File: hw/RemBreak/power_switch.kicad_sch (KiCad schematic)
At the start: 33 parts, among them IC1 LTC2943IDD#TRPBF, IC2 MAX17049G+T10, Q10 BC337, Q11 BC847, Q12 Si7141DP, Q13 BC337, Q14 BC847, U2 INA219BxDCN, U6 BD4830FVE-TR

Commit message: reorganized subsheets
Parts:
- removed C1: 0.1uF, symbol Device:C_Polarized
- removed C5: 100nF, symbol Device:C
- removed IC1: LTC2943IDD#TRPBF, SON50P300X300X80-9N-D, symbol dodo-device:LTC2943IDD#TRPBF
- removed IC2: MAX17049G+T10, Package_DFN_QFN:TDFN-8-1EP_2x2mm_P0.5mm_EP0.8x1.2mm, symbol dodo-power:MAX17049G+T10
- removed R16, R18: 10, symbol Device:R
- removed R19, R23: 10k, symbol Device:R
- removed U2: INA219BxDCN, Package_TO_SOT_SMD:SOT-23-8, symbol Analog_ADC:INA219BxDCN
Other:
- note removed: "BATTERY SoC IC I2C address: 0x36 + R/W"
- note removed: "CURRENT SENSOR I2C address: 0x40 + R/W"

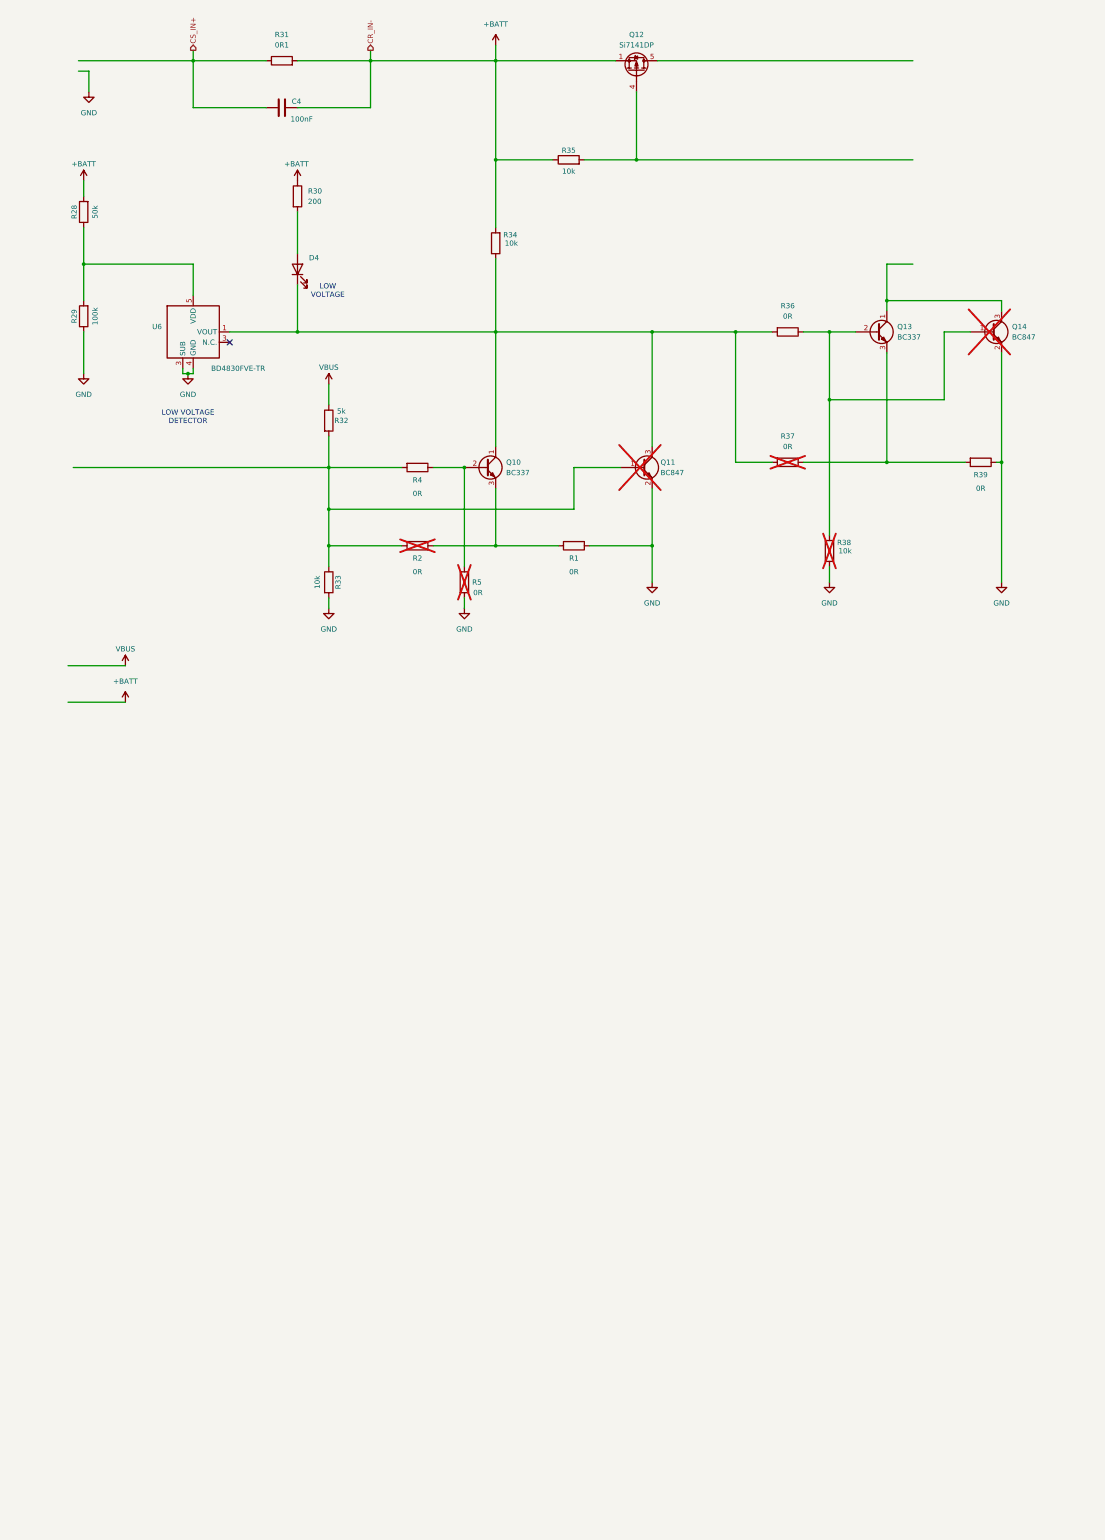
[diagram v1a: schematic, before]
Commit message: project update - started drawing the first revision of the board
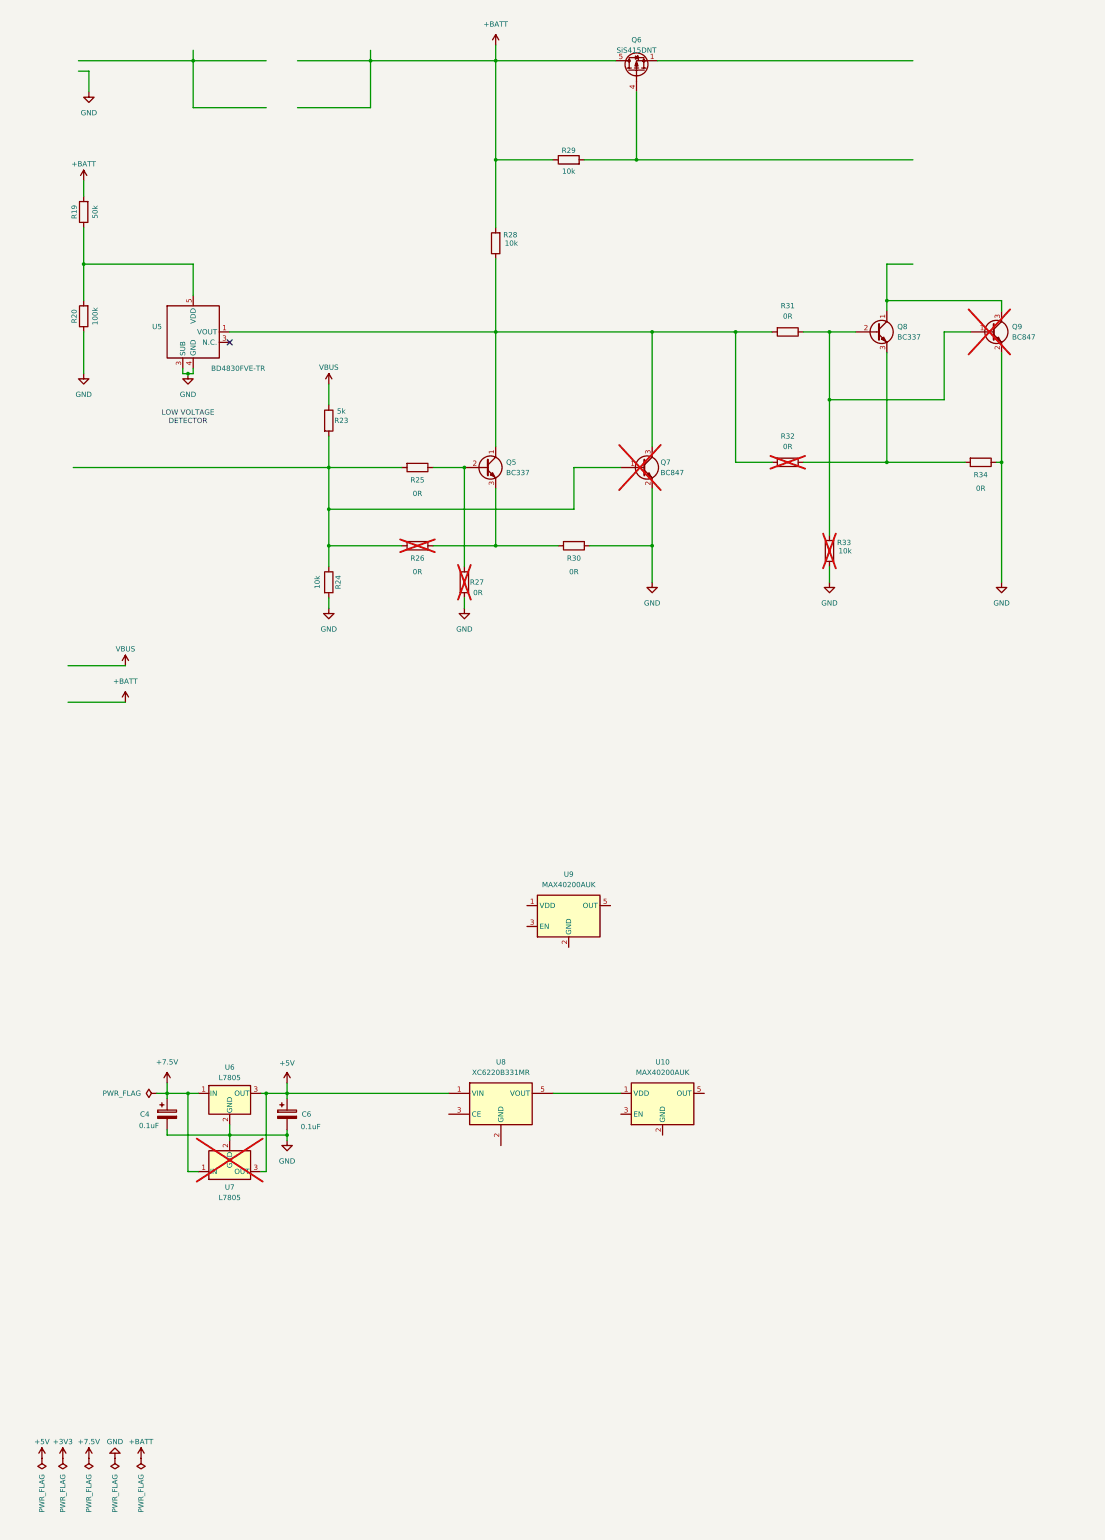
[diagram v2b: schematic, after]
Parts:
- removed C4: 100nF, symbol Device:C
- removed D4: LED, symbol Device:LED
- removed Q12: Si7141DP, Package_SO:PowerPAK_SO-8_Single, symbol Transistor_FET:Si7141DP
- removed R30: 200, symbol Device:R
- removed R31: 0R1, symbol Device:R
- added C4, C6: 0.1uF, Capacitor_SMD:C_0805_2012Metric, symbol Device:C_Polarized
- added Q6: SiS415DNT, Package_SO:Vishay_PowerPAK_1212-8_Single, symbol Transistor_FET:SiS415DNT
- added U10, U9: MAX40200AUK, Package_TO_SOT_SMD:SOT-23-5, symbol Analog_Switch:MAX40200AUK
- added U6: L7805, Package_TO_SOT_SMD:TO-263-2, symbol Regulator_Linear:L7805
- added U7: L7805, Package_TO_SOT_THT:TO-220-3_Horizontal_TabDown, symbol Regulator_Linear:L7805
- added U8: XC6220B331MR, Package_TO_SOT_SMD:SOT-23-5, symbol Regulator_Linear:XC6220B331MR
- R19: renamed from R28; footprint (none) -> Resistor_SMD:R_0805_2012Metric
- R20: renamed from R29; footprint (none) -> Resistor_SMD:R_0805_2012Metric
- R23: renamed from R32; footprint (none) -> Resistor_SMD:R_0805_2012Metric
- R24: renamed from R33; footprint (none) -> Resistor_SMD:R_0805_2012Metric
- R25: renamed from R4; footprint (none) -> Resistor_SMD:R_0805_2012Metric
- R26: renamed from R2; footprint (none) -> Resistor_SMD:R_0805_2012Metric
- R27: renamed from R5; footprint (none) -> Resistor_SMD:R_0805_2012Metric
- R28: renamed from R34; footprint (none) -> Resistor_SMD:R_0805_2012Metric
- R29: renamed from R35; footprint (none) -> Resistor_SMD:R_0805_2012Metric
- R30: renamed from R1; footprint (none) -> Resistor_SMD:R_0805_2012Metric
- R31: renamed from R36; footprint (none) -> Resistor_SMD:R_0805_2012Metric
- R32: renamed from R37; footprint (none) -> Resistor_SMD:R_0805_2012Metric
- R33: renamed from R38; footprint (none) -> Resistor_SMD:R_0805_2012Metric
- R34: renamed from R39; footprint (none) -> Resistor_SMD:R_0805_2012Metric
- renumbered Q10 to Q5, Q11 to Q7, Q13 to Q8, Q14 to Q9, U6 to U5
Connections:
- net +BATT: now also Q6.5 (D)
- net GND: now also C4.2, C6.2, U6.2 (GND), U7.2 (GND)
- net at R29.2: now also Q6.4 (G)
- new net: Q6.1 (S), Q6.2 (S), Q6.3 (S)
- new net: U10.1 (VDD), U8.5 (VOUT)
- new net +5V: C6.1, U6.3 (OUT), U7.3 (OUT), U8.1 (VIN)
- new net +7.5V: C4.1, U6.1 (IN), U7.1 (IN)
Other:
- note removed: "LOW VOLTAGE"

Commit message: schematics drawing in progress
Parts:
- removed C4, C6: 0.1uF, Capacitor_SMD:C_0805_2012Metric, symbol Device:C_Polarized
- removed Q7: BC847, Package_TO_SOT_SMD:SOT-23, symbol Transistor_BJT:BC847
- removed Q8: BC337, Package_TO_SOT_THT:TO-92_Inline, symbol Transistor_BJT:BC337
- removed R23: 5k, Resistor_SMD:R_0805_2012Metric, symbol Device:R
- removed R24, R28, R29: 10k, Resistor_SMD:R_0805_2012Metric, symbol Device:R
- removed U10, U9: MAX40200AUK, Package_TO_SOT_SMD:SOT-23-5, symbol Analog_Switch:MAX40200AUK
- removed U5: BD4830FVE-TR, Package_TO_SOT_SMD:VSOF5, symbol dodo-power:BD4830FVE-TR
- removed U6: L7805, Package_TO_SOT_SMD:TO-263-2, symbol Regulator_Linear:L7805
- removed U7: L7805, Package_TO_SOT_THT:TO-220-3_Horizontal_TabDown, symbol Regulator_Linear:L7805
- removed U8: XC6220B331MR, Package_TO_SOT_SMD:SOT-23-5, symbol Regulator_Linear:XC6220B331MR
- added J12, J14: Conn_01x01, TestPoint:TestPoint_Pad_2.5x2.5mm, symbol Connector_Generic:Conn_01x01
- added Q6: BC847, Package_TO_SOT_SMD:SOT-23, symbol Transistor_BJT:BC847
- added Q9: BC337, Package_TO_SOT_THT:TO-92_Inline, symbol Transistor_BJT:BC337
- added R26, R27: 10k, Resistor_SMD:R_0805_2012Metric, symbol Device:R
- added U8, U9: BD48ExxG, Package_TO_SOT_SMD:SOT-23-5, symbol Power_Management:BD48ExxG
- R25: value 0R -> 10k
- R30: value 0R -> 47k
- R31: now not fitted
- R33: value 10k -> 0R; now fitted
- renumbered Q9 to Q10, Q5 to Q7, Q6 to Q8, R19 to R23, R20 to R24, R27 to R28, R26 to R29
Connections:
- net GND: now also Q7.3 (E), Q6.2 (E), Q9.3 (E), U8.3 (GND), U9.3 (GND); no longer Q10.2 (E), R30.1, R33.1, R34.1
- net VBUS: now also R30.2, U9.2 (VDD)
- net at R29.2: no longer R25.2
- net at R23.1, R24.2: now also U8.2 (VDD)
- net at R34.2: now also R32.2, Q6.3 (C), Q9.1 (C); no longer R32.1
- net at Q7.2 (B), R25.1: now also R31.1, R34.1, U8.1 (VOUT); no longer R28.1
- net SERVO_pwr: now reaches Q8.1 (S), Q8.2 (S), Q8.3 (S)
- net at Q8.4 (G): now also R26.2, R27.2
- net +BATT renamed PWR
- net PWR: now also R25.2, J12.1 (Pin_1); no longer Q8.5 (D)
- new net: Q6.1 (B), Q9.2 (B), R28.1, R31.2, R33.2
- new net: Q7.1 (C), R27.1
- new net EN: R30.1, R32.1, R33.1, U9.1 (VOUT)
- new net VBATT: J14.1 (Pin_1), Q8.5 (D), R26.1
- now unconnected: Q10.1 (B), R29.1
- no-connect marks 1 -> 0
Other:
- note added: "SWITCH ON/OFF"
- note added: "VBUS > 3.5V -> VOUT = VBUS VBUS <3.0V -> VOUT = GND"
- moved on the sheet: Q10, Q7, Q8, R23, R24, R28, R29

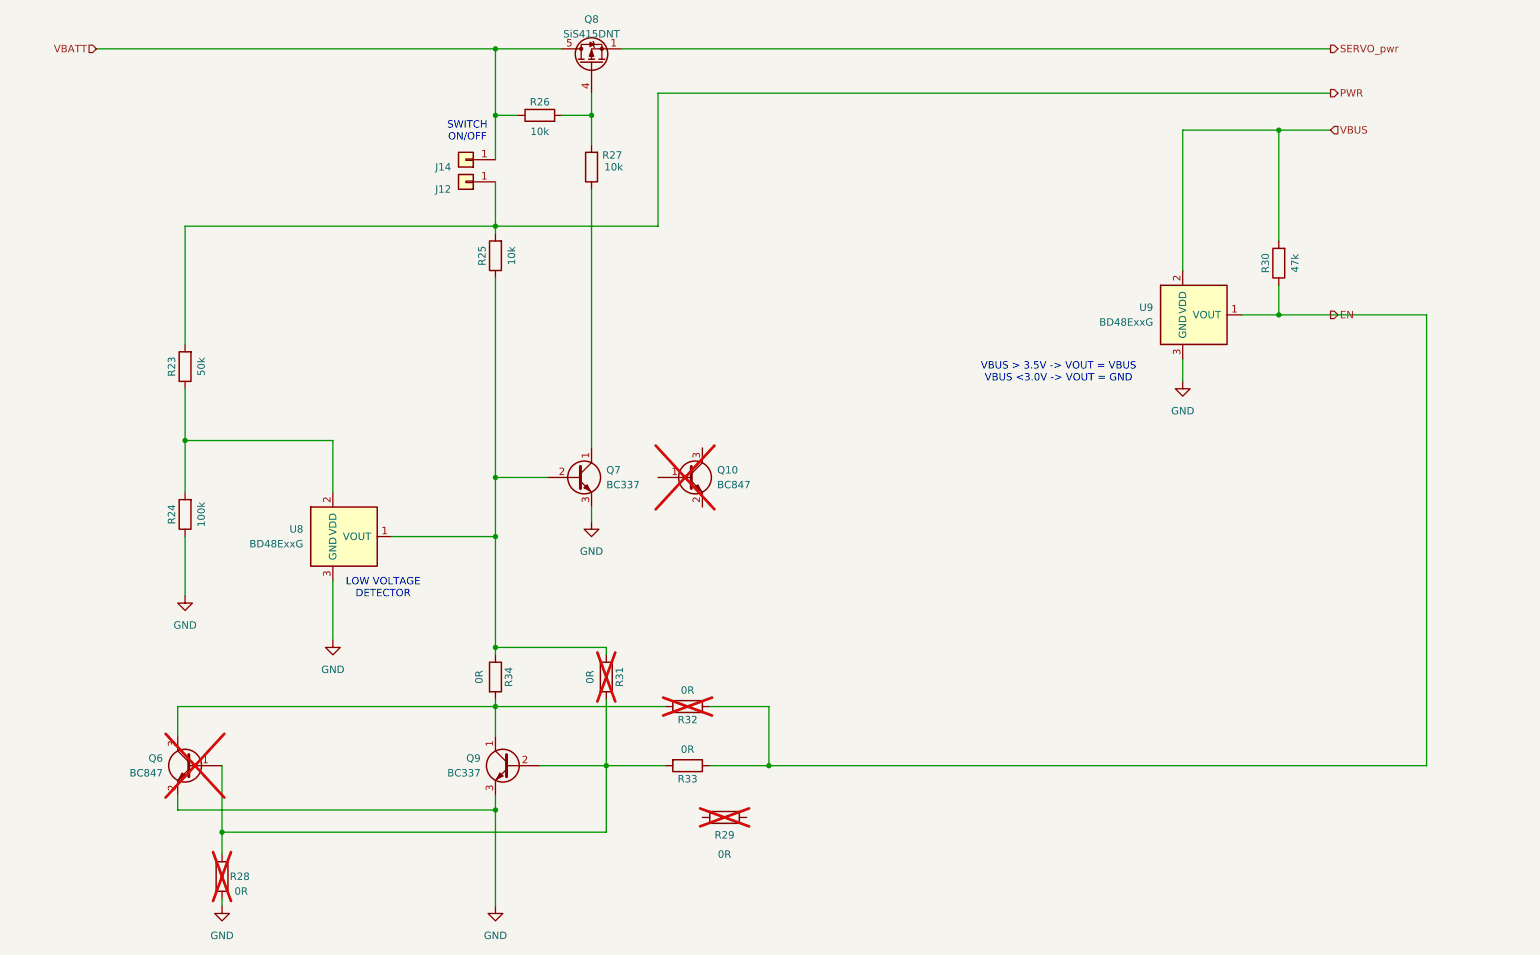
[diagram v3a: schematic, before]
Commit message: changes in power line sharing in progress
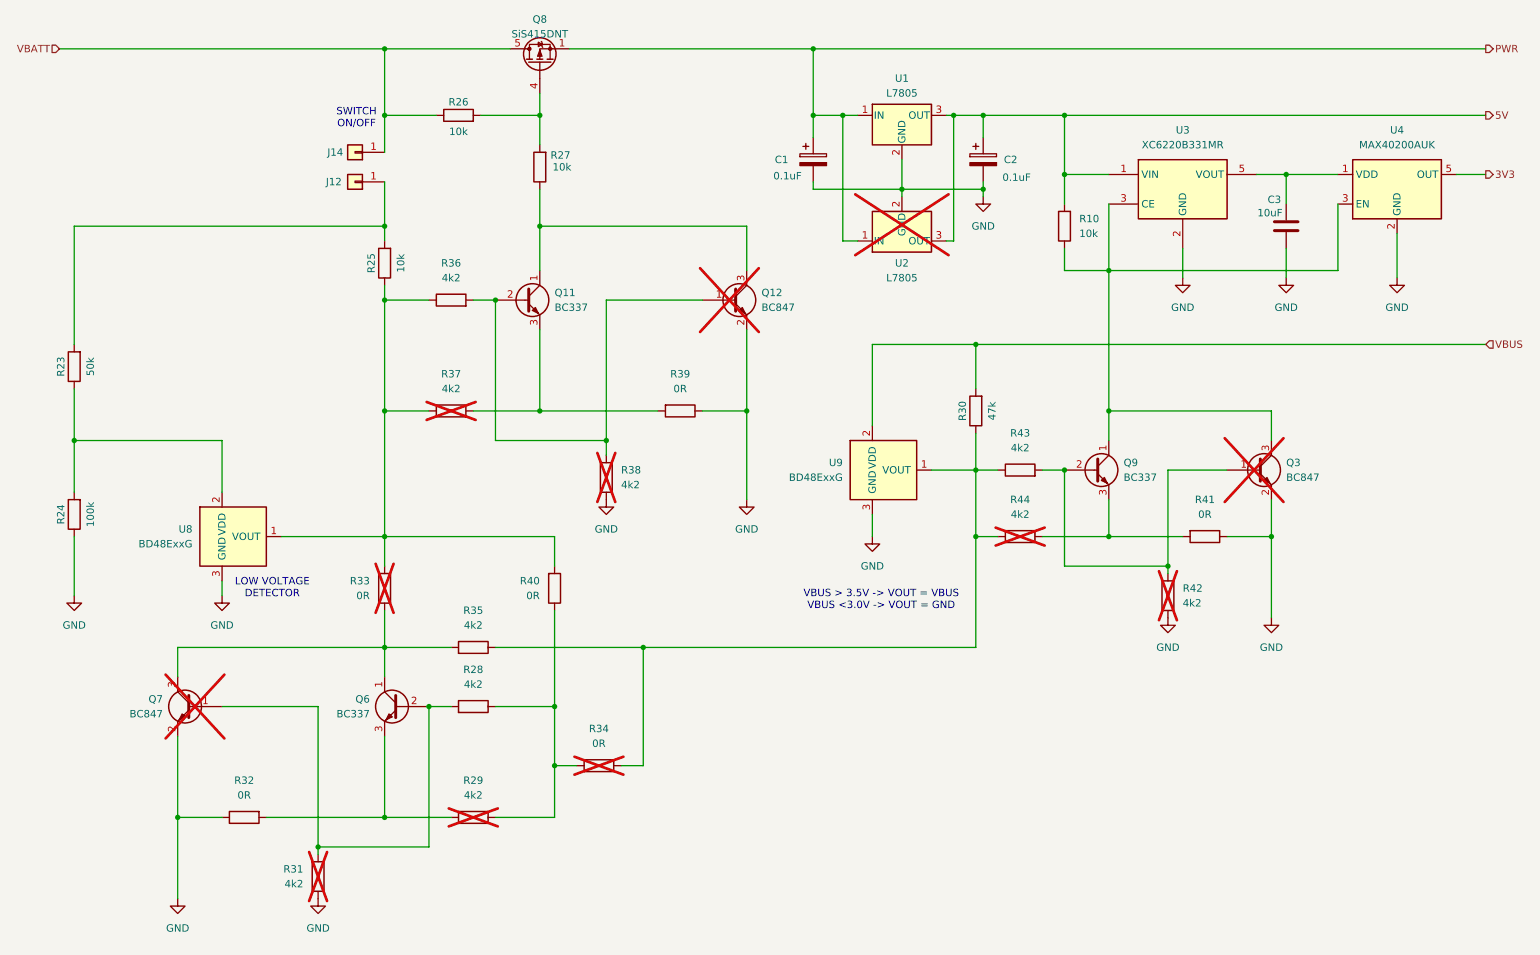
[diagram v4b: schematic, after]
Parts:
- removed Q10, Q6: BC847, Package_TO_SOT_SMD:SOT-23, symbol Transistor_BJT:BC847
- removed Q7: BC337, Package_TO_SOT_THT:TO-92_Inline, symbol Transistor_BJT:BC337
- added C1, C2: 0.1uF, Capacitor_SMD:C_0805_2012Metric, symbol Device:C_Polarized
- added C3: 10uF, Capacitor_SMD:C_0805_2012Metric, symbol Device:C
- added Q11, Q6: BC337, Package_TO_SOT_THT:TO-92_Inline, symbol Transistor_BJT:BC337
- added Q12, Q3, Q7: BC847, Package_TO_SOT_SMD:SOT-23, symbol Transistor_BJT:BC847
- added R10: 10k, Resistor_SMD:R_0805_2012Metric, symbol Device:R
- added R35, R36, R37, R38, R42, R43, R44: 4k2, Resistor_SMD:R_0805_2012Metric, symbol Device:R
- added R39, R40, R41: 0R, Resistor_SMD:R_0805_2012Metric, symbol Device:R
- added U1: L7805, Package_TO_SOT_SMD:TO-263-2, symbol Regulator_Linear:L7805
- added U2: L7805, Package_TO_SOT_THT:TO-220-3_Horizontal_TabDown, symbol Regulator_Linear:L7805
- added U3: XC6220B331MR, Package_TO_SOT_SMD:SOT-23-5, symbol Regulator_Linear:XC6220B331MR
- added U4: MAX40200AUK, Package_TO_SOT_SMD:SOT-23-5, symbol Analog_Switch:MAX40200AUK
- R28: value 0R -> 4k2; now fitted
- R29, R31: value 0R -> 4k2
- R32: now fitted
- R33, R34: now not fitted
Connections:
- net SERVO_pwr is gone; now on net PWR: Q8.1 (S), Q8.2 (S), Q8.3 (S)
- net GND: now also R31.1, R32.1, C1.2, C2.2, C3.2, Q12.2 (E), Q3.2 (E), Q7.2 (E), R38.1, R39.1, R41.1, R42.1, U1.2 (GND), U2.2 (GND), U3.2 (GND), U4.2 (GND); no longer Q9.3 (E), R28.2
- net PWR: now also C1.1, U1.1 (IN), U2.1 (IN); no longer J12.1 (Pin_1), R23.2, R25.2
- net at R29.1: now also R28.1, R34.2, R40.1
- net at R29.2: now also R32.2, Q6.3 (E)
- net at R25.1, U8.1 (VOUT): now also R33.2, R36.1, R37.1, R40.2; no longer R31.1, R34.1
- net at R27.1: now also Q11.1 (C), Q12.3 (C)
- net EN: no longer names the net of R30.1, U9.1 (VOUT)
- net EN: now also R34.1, R35.1, R43.1, R44.1; no longer R32.1, R33.1
- new net: Q11.2 (B), Q12.1 (B), R36.2, R38.2
- new net: Q11.3 (E), R37.2, R39.2
- new net: J12.1 (Pin_1), R23.2, R25.2
- new net: Q3.1 (B), Q9.2 (B), R42.2, R43.2
- new net: C3.1, U3.5 (VOUT), U4.1 (VDD)
- new net: Q6.1 (C), Q7.3 (C), R33.1, R35.2
- new net: Q3.3 (C), Q9.1 (C), R10.1, U3.3 (CE), U4.3 (EN)
- new net: Q6.2 (B), Q7.1 (B), R28.2, R31.2
- new net: Q9.3 (E), R41.2, R44.2
- new net 3V3: U4.5 (OUT)
- new net 5V: C2.1, R10.2, U1.3 (OUT), U2.3 (OUT), U3.1 (VIN)
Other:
- moved on the sheet: J12, J14, Q8, R23, R24, R25, R26, R27, R30, U8, U9
